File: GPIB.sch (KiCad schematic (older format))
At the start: 10 parts

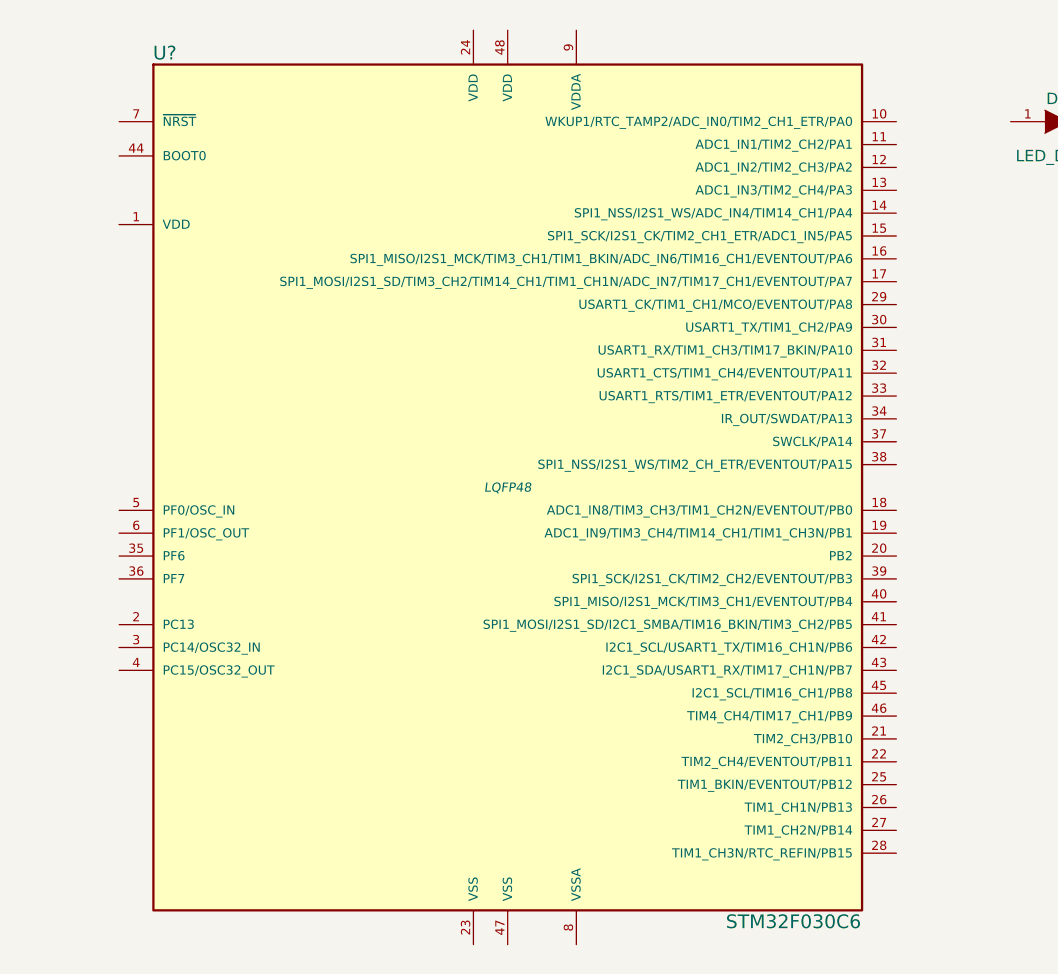
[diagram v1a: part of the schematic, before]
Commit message: More cleanup and swap out M0 model
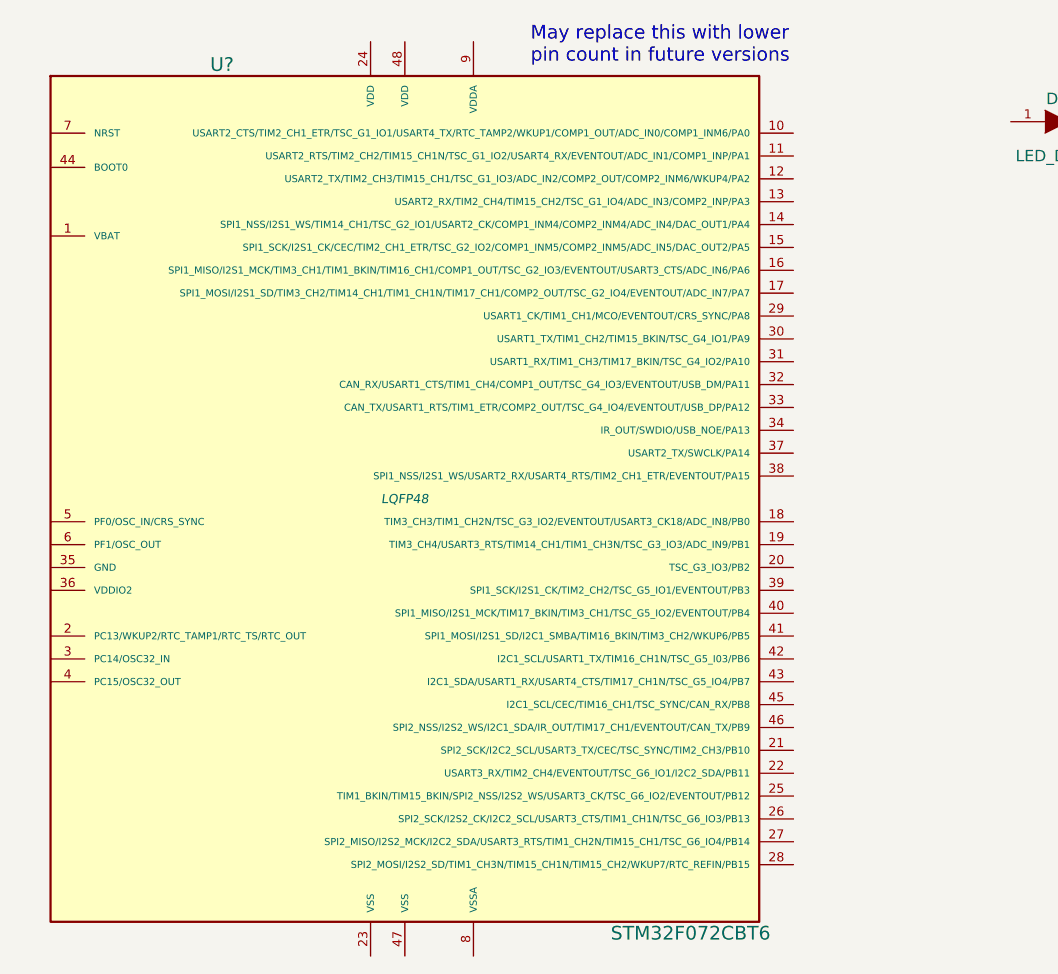
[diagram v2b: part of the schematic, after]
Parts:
- removed U?: STM32F030C6, LQFP48, symbol STM32F030C6
- added U?: STM32F072CBT6, LQFP48, symbol STM32F072CBT6
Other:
- note added: "May replace this with lower\npin count in future versions"
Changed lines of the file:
@@
 LIBS:irlml2246tr
 LIBS:testpoint
+LIBS:vin
+LIBS:stm32f072cbt6
 LIBS:Wifi-GPIB-cache
 EELAYER 25 0
@@
 Comment4 ""
 $EndDescr
-$Comp
-L STM32F030C6 U?
-U 1 1 55668602
-P 2700 3900
-F 0 "U?" H 1200 5800 60  0000 C CNN
-F 1 "STM32F030C6" H 3950 2000 60  0000 C CNN
-F 2 "LQFP48" H 2700 3900 40  0000 C CIN
-F 3 "" H 2700 3900 60  0000 C CNN
-	1    2700 3900
-	1    0    0    -1
-$EndComp
 $Comp
 L SN75160B U?
@@
 	1    0    0    -1
 $EndComp
+$Comp
+L STM32F072CBT6 U?
+U 1 1 55677971
+P 2250 3950
+F 0 "U?" H 1450 5850 60  0000 C CNN
+F 1 "STM32F072CBT6" H 3500 2050 60  0000 C CNN
+F 2 "LQFP48" H 2250 3950 40  0000 C CIN
+F 3 "" H 2250 3950 60  0000 C CNN
+	1    2250 3950
+	1    0    0    -1
+$EndComp
+Text Notes 2800 2050 0    60   ~ 0
+May replace this with lower\npin count in future versions
 $EndSCHEMATC

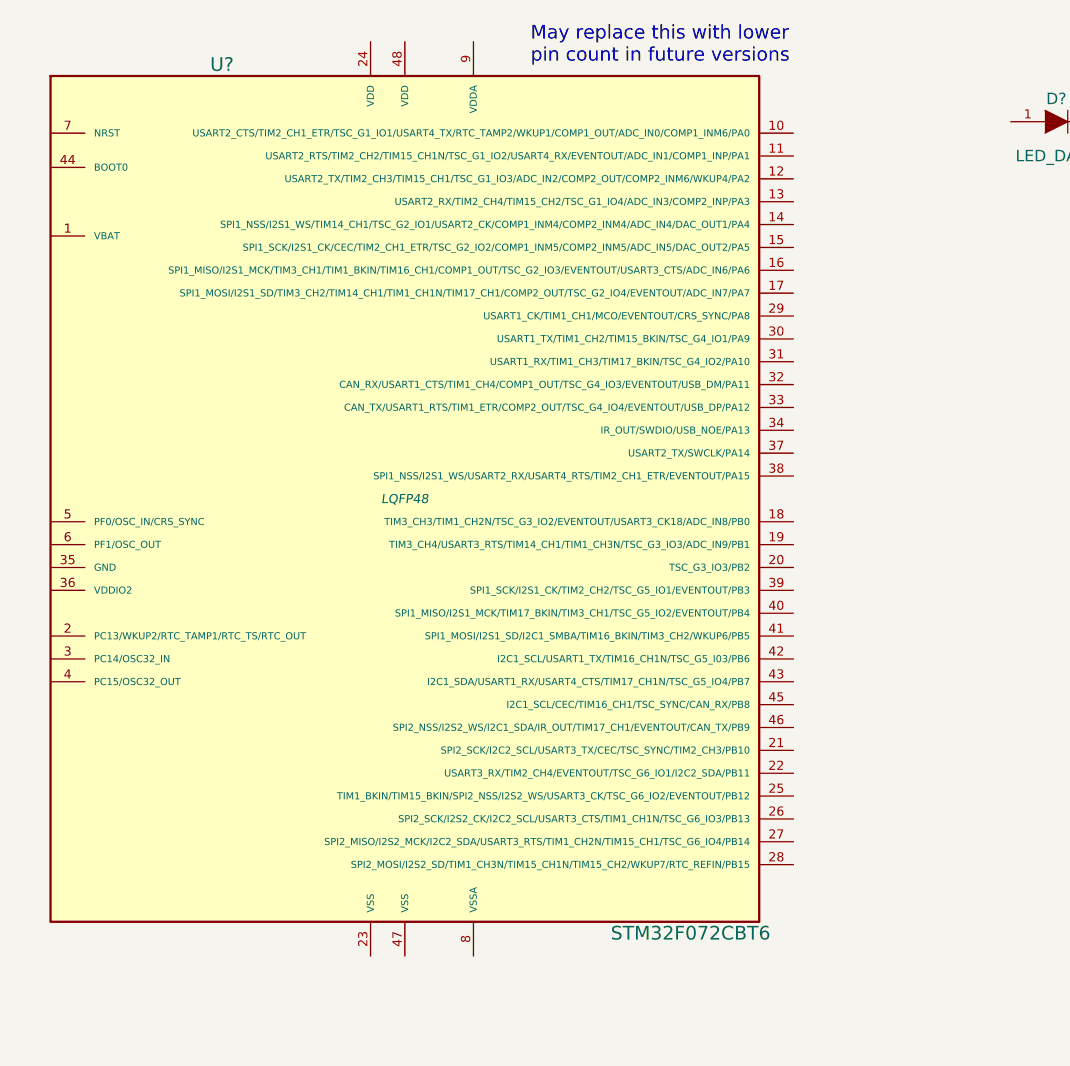
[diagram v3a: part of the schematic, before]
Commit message: Add new stm32f072 to sch
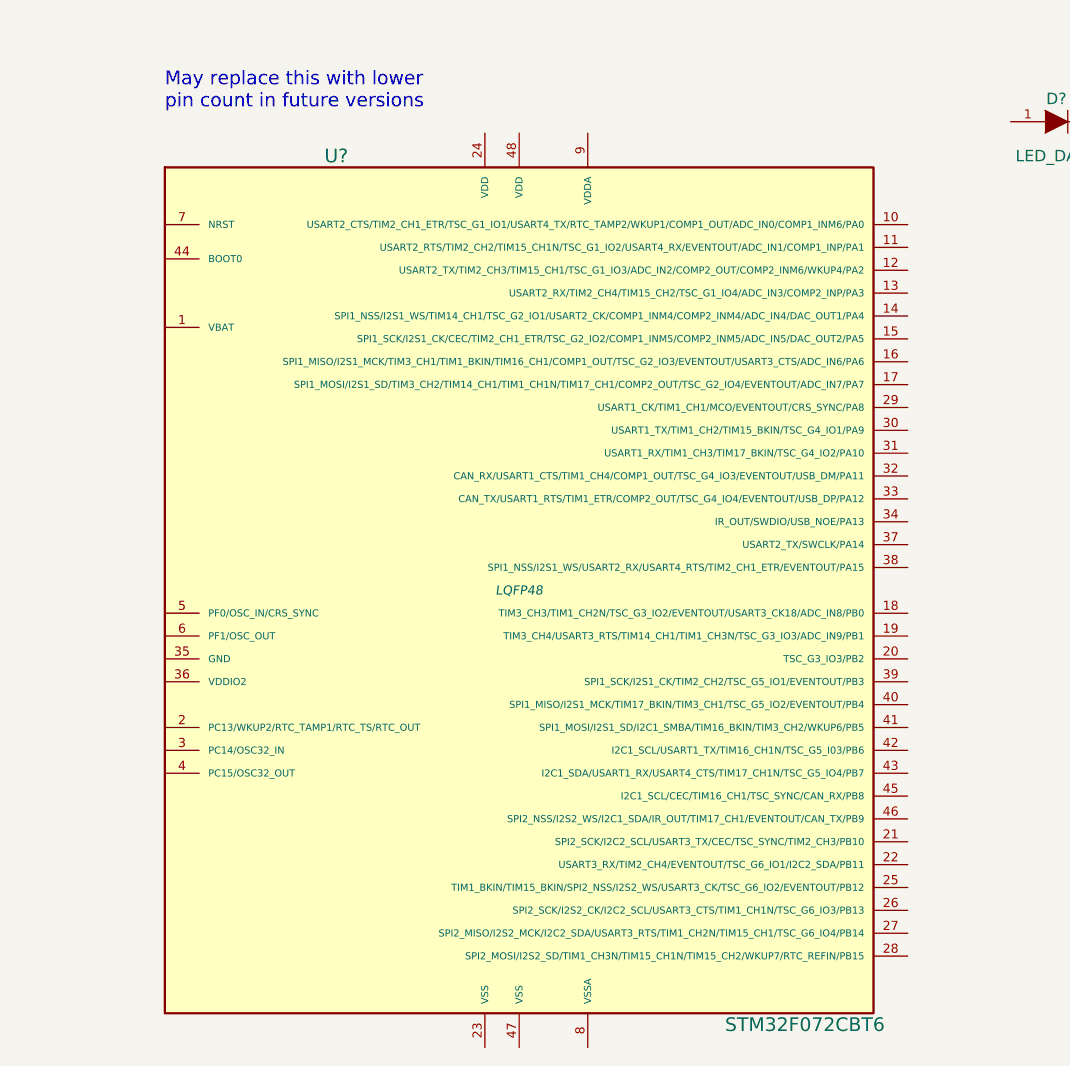
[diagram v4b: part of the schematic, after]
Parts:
- removed U?: STM32F072CBT6, LQFP48, symbol STM32F072CBT6
- added U?: STM32F072CBT6, LQFP48, symbol STM32F072CBT6
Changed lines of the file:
@@
 LIBS:SN75160B
 LIBS:SN75162B
-LIBS:stm32f030c6
 LIBS:conn_centronics_24
 LIBS:open-project
@@
 LIBS:vin
 LIBS:stm32f072cbt6
-LIBS:nuf2221w1
 LIBS:Wifi-GPIB-cache
 EELAYER 25 0
@@
 	1    0    0    -1
 $EndComp
+Text Notes 1200 2250 0    60   ~ 0
+May replace this with lower\npin count in future versions
 $Comp
 L STM32F072CBT6 U?
-U 1 1 55677971
-P 2250 3950
-F 0 "U?" H 1450 5850 60  0000 C CNN
-F 1 "STM32F072CBT6" H 3500 2050 60  0000 C CNN
-F 2 "LQFP48" H 2250 3950 40  0000 C CIN
-F 3 "" H 2250 3950 60  0000 C CNN
-	1    2250 3950
+U 1 1 5567A2FB
+P 2750 4350
+F 0 "U?" H 1950 6250 60  0000 C CNN
+F 1 "STM32F072CBT6" H 4000 2450 60  0000 C CNN
+F 2 "LQFP48" H 2750 4350 40  0000 C CIN
+F 3 "" H 2750 4350 60  0000 C CNN
+	1    2750 4350
 	1    0    0    -1
 $EndComp
-Text Notes 2800 2050 0    60   ~ 0
-May replace this with lower\npin count in future versions
 $EndSCHEMATC

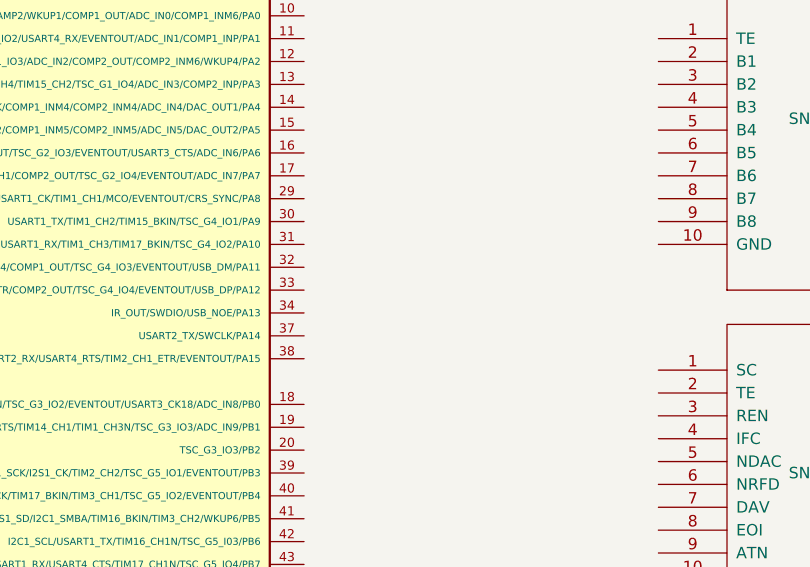
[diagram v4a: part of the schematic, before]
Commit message: Connect up USB pins
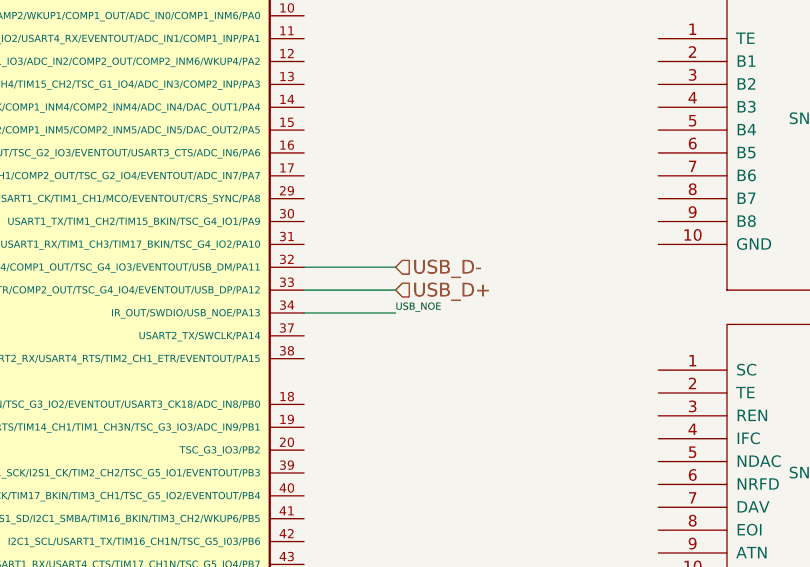
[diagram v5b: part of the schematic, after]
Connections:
- net USB_D-: now reaches U?.32 (CAN_RX/USART1_CTS/TIM1_CH4/COMP1_OUT/TSC_G4_IO3/EVENTOUT/USB_DM/PA11)
- net USB_D+: now reaches U?.33 (CAN_TX/USART1_RTS/TIM1_ETR/COMP2_OUT/TSC_G4_IO4/EVENTOUT/USB_DP/PA12)
- net USB_NOE: now reaches U?.34 (IR_OUT/SWDIO/USB_NOE/PA13)
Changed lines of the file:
@@
 	1    0    0    -1
 $EndComp
+Wire Wire Line
+	4450 4050 4850 4050
+Text Label 4850 4050 0    31   ~ 0
+USB_NOE
+Wire Wire Line
+	4450 3950 4850 3950
+Wire Wire Line
+	4450 3850 4850 3850
+Text HLabel 4850 3850 2    60   Input ~ 0
+USB_D-
+Text HLabel 4850 3950 2    60   Input ~ 0
+USB_D+
 $EndSCHEMATC

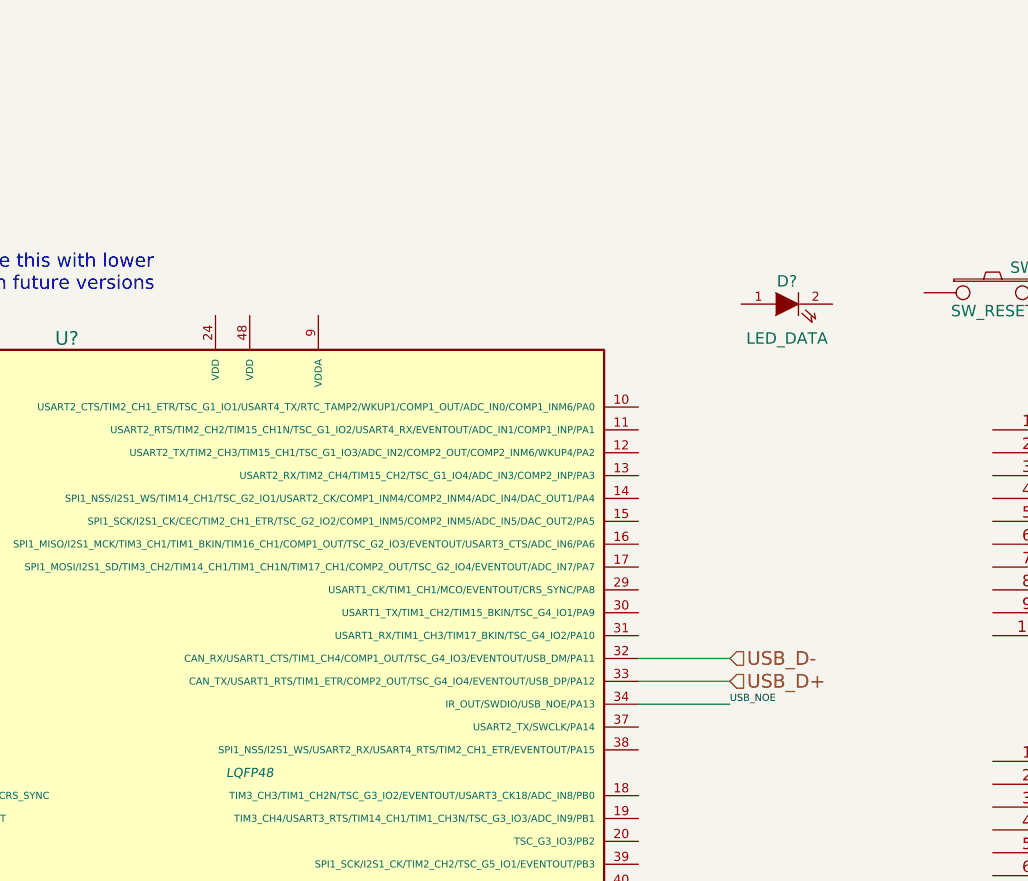
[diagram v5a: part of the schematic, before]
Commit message: Add USB activity LED
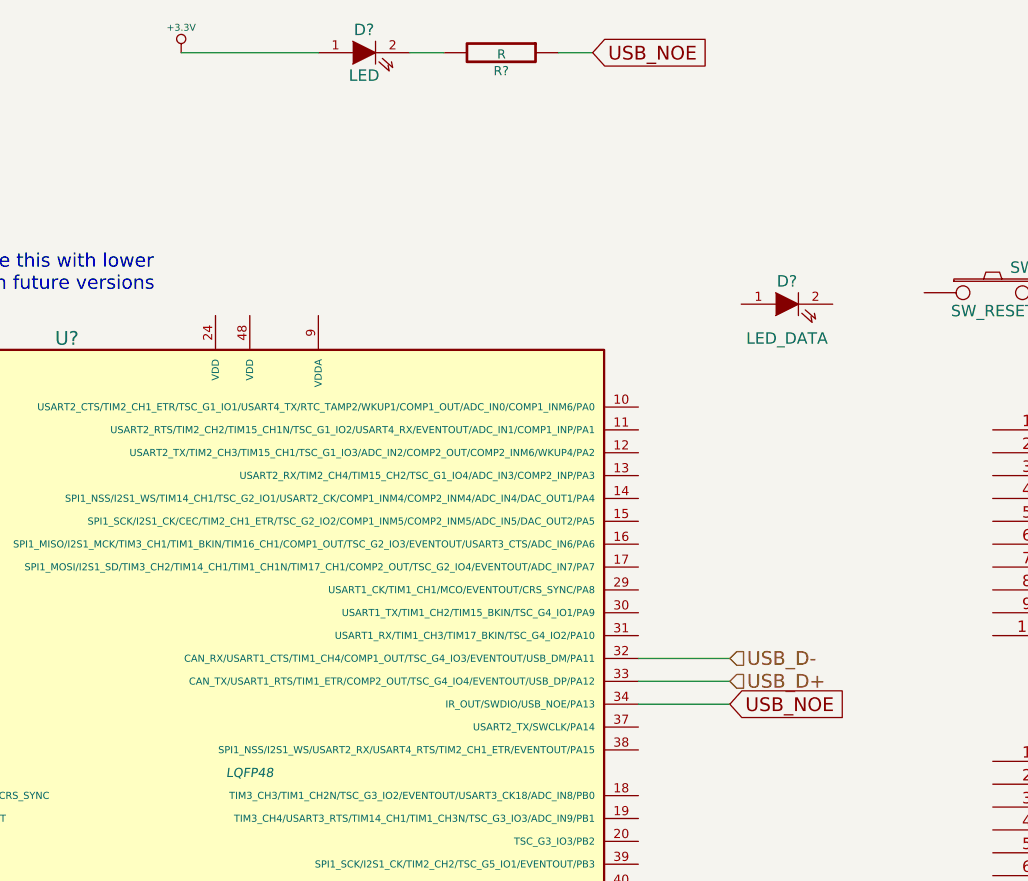
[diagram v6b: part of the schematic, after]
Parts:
- added D?: LED, symbol LED
- added R?: R, symbol R
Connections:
- net USB_NOE: now also R?.1
- new net: D?.2 (K), R?.2
- new net +3.3V: D?.1 (A)
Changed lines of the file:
@@
 Wire Wire Line
 	4450 4050 4850 4050
-Text Label 4850 4050 0    31   ~ 0
-USB_NOE
 Wire Wire Line
 	4450 3950 4850 3950
@@
 Text HLabel 4850 3950 2    60   Input ~ 0
 USB_D+
+$Comp
+L LED D?
+U 1 1 5567B154
+P 3250 1200
+F 0 "D?" H 3250 1300 50  0000 C CNN
+F 1 "LED" H 3250 1100 50  0000 C CNN
+F 2 "" H 3250 1200 60  0000 C CNN
+F 3 "" H 3250 1200 60  0000 C CNN
+	1    3250 1200
+	1    0    0    -1
+$EndComp
+$Comp
+L +3.3V #PWR?
+U 1 1 5567B18B
+P 2450 1200
+F 0 "#PWR?" H 2450 1160 30  0001 C CNN
+F 1 "+3.3V" H 2450 1310 30  0000 C CNN
+F 2 "" H 2450 1200 60  0000 C CNN
+F 3 "" H 2450 1200 60  0000 C CNN
+	1    2450 1200
+	1    0    0    -1
+$EndComp
+Wire Wire Line
+	2450 1200 3050 1200
+$Comp
+L R R?
+U 1 1 5567B1D4
+P 3850 1200
+F 0 "R?" V 3930 1200 40  0000 C CNN
+F 1 "R" V 3857 1201 40  0000 C CNN
+F 2 "" V 3780 1200 30  0000 C CNN
+F 3 "" H 3850 1200 30  0000 C CNN
+	1    3850 1200
+	0    1    1    0
+$EndComp
+Wire Wire Line
+	3450 1200 3600 1200
+Wire Wire Line
+	4100 1200 4250 1200
+Text GLabel 4850 4050 2    60   Input ~ 0
+USB_NOE
+Text GLabel 4250 1200 2    60   Input ~ 0
+USB_NOE
 $EndSCHEMATC
